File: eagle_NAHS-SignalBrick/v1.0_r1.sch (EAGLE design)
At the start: 42 parts, among them IC1 ESP12F, IC2 ATTINY212-SSNR, IC3 TP4056, IC4 DW01A, J1 10118194-0001LF, J2 Brick-Interface, Q1 8205A

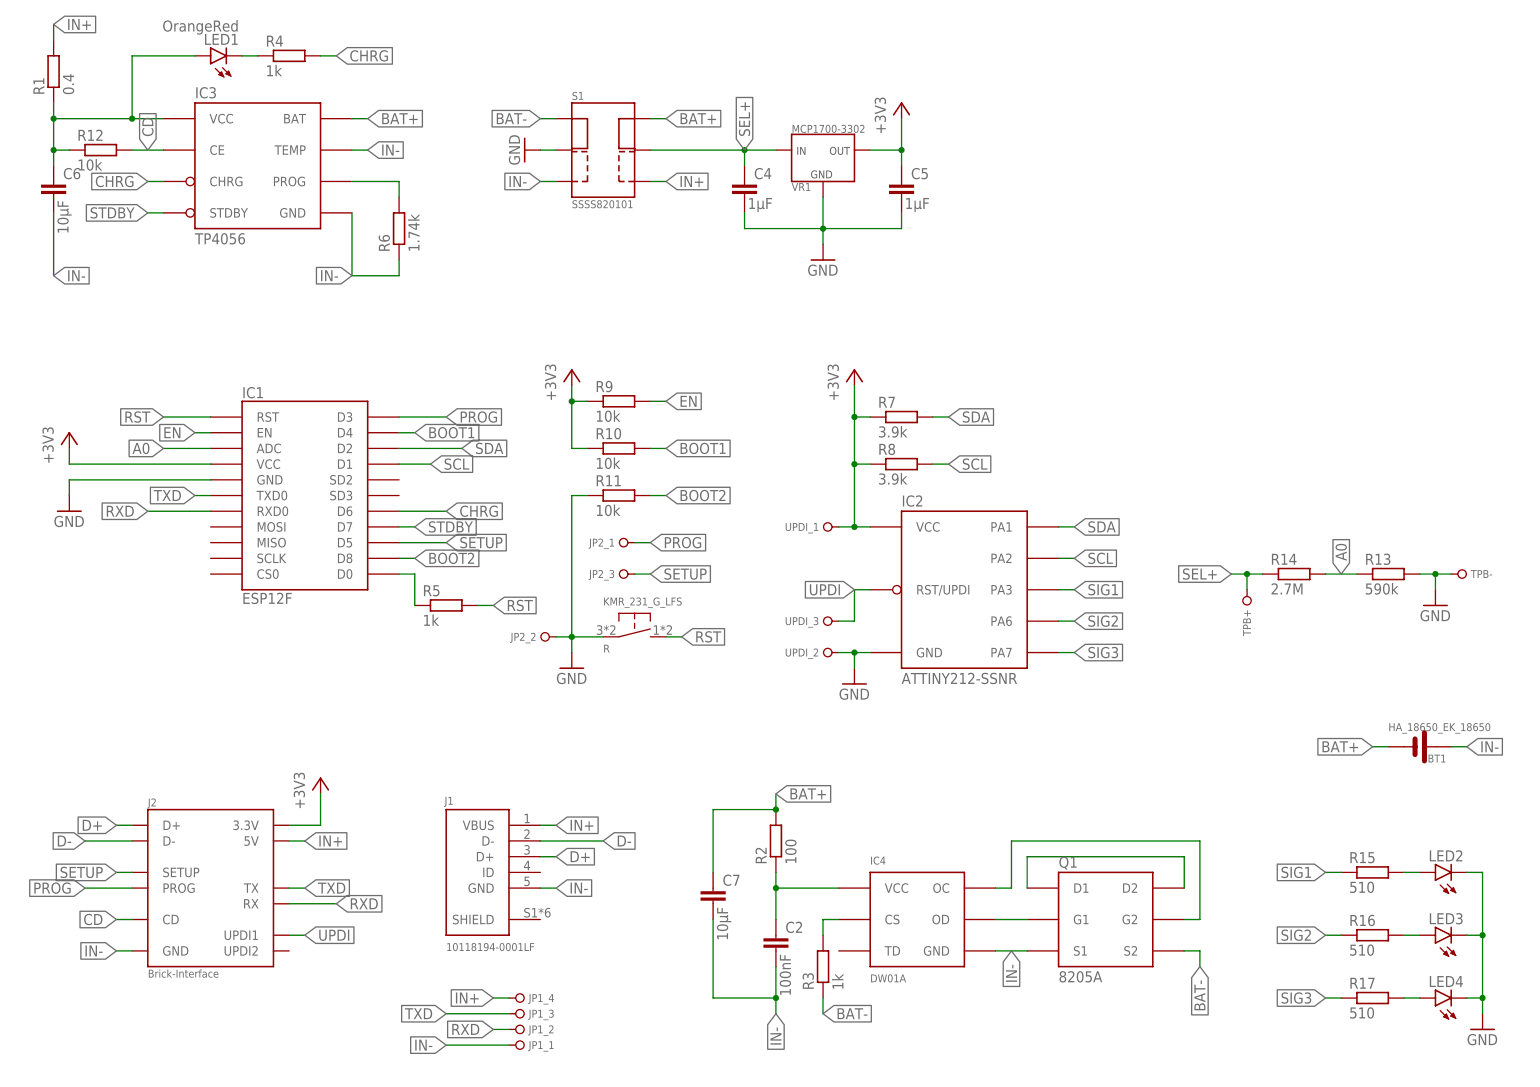
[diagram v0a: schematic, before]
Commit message: renamed components, finished for production
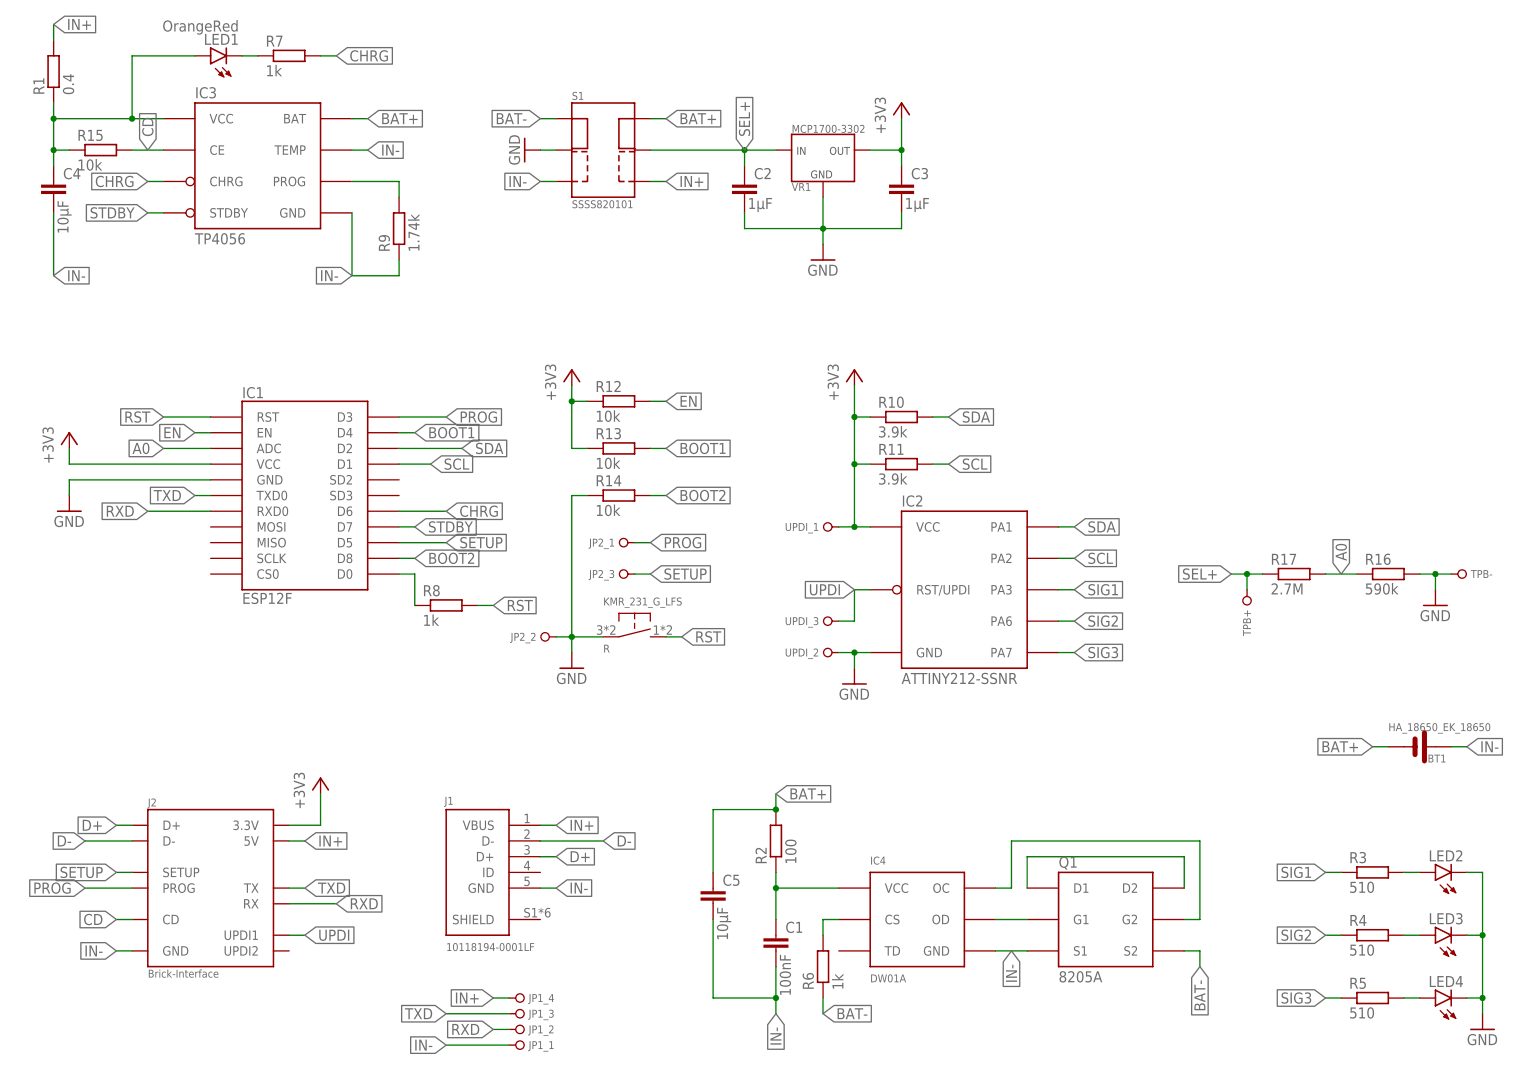
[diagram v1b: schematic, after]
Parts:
- removed C6, C7: 10µF, rcl:C-EUC0805
- added C1: 100nF, rcl:C-EUC0805
- added C3: 1µF, rcl:C-EUC0805
- C2: value 100nF -> 1µF
- C4, C5: value 1µF -> 10µF
- R10, R11: value 10k -> 3.9k
- R13: value 590k -> 10k
- R14: value 2.7M -> 10k
- R15: value 510 -> 10k; device rcl:R-EU_R0603 -> rcl:R-EU_R0805
- R16: value 510 -> 590k; device rcl:R-EU_R0603 -> rcl:R-EU_R0805
- R17: value 510 -> 2.7M; device rcl:R-EU_R0603 -> rcl:R-EU_R0805
- R3, R4, R5: value 1k -> 510; device rcl:R-EU_R0805 -> rcl:R-EU_R0603
- R6: value 1.74k -> 1k
- R7, R8: value 3.9k -> 1k
- R9: value 10k -> 1.74k
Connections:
- net +3V3: now also C3.1, R11.1, R12.1, R13.1; no longer C5.1, R7.1, R8.1, R9.1
- net A0: now also R16.1, R17.2; no longer R13.1, R14.2
- net BAT+: now also C5.1; no longer C7.1
- net BAT-: now also R6.1; no longer R3.1
- net BOOT1: now also R13.2; no longer R10.2
- net BOOT2: now also R14.2; no longer R11.2
- net CD: now also R15.2; no longer R12.2
- net CHRG: now also R7.2; no longer R4.2
- net EN: now also R12.2; no longer R9.2
- net GND: now also C2.2, C3.2, R14.1, R16.2; no longer C4.2, C5.2, R11.1, R13.2
- net IN-: now also C1.2, C4.2, C5.2, R9.1; no longer C2.2, C6.2, C7.2, R6.1
- net N$1: now also C4.1, R15.1; no longer C6.1, R12.1
- net N$2: now also R9.2; no longer R6.2
- net N$3: now also R6.2; no longer R3.2
- net N$4: now also C1.1; no longer C2.1
- net N$5: now also R3.2; no longer R15.2
- net N$6: now also R4.2; no longer R16.2
- net N$7: now also R7.1; no longer R4.1
- net N$9: now also R5.2; no longer R17.2
- net RST: now also R8.2; no longer R5.2
- net SCL: now also R11.2; no longer R8.2
- net SDA: now also R10.2; no longer R7.2
- net SEL+: now also C2.1, R17.1; no longer C4.1, R14.1
- net SIG1: now also R3.1; no longer R15.1
- net SIG2: now also R4.1; no longer R16.1
- net SIG3: now also R5.1; no longer R17.1
- net WAKE: now also R8.1; no longer R5.1
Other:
- moved on the sheet: C2, C4, C5, R10, R11, R12, R13, R14, R15, R16, R17, R3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
